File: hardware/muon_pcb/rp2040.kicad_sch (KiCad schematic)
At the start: 38 parts, among them J4 Micro_SD_Card_Det1, J5 Conn_01x02_Pin, SW4 SW_Push_Shielded, SW5 SW_Push_Shielded, U12 RP2040, U3 W25Q128JVS, Y3 ABM8-272-T3

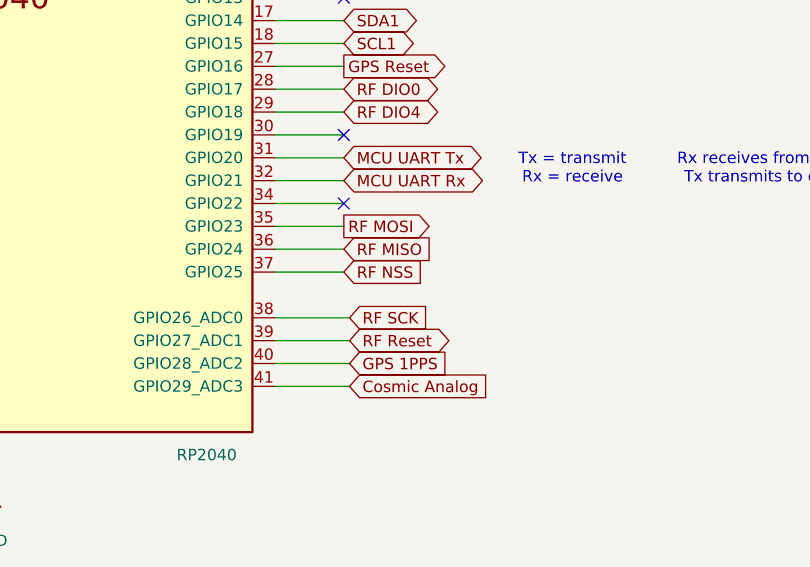
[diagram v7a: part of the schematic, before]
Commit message: cleaned up schematic & implemented changes to layout
to do (off top of my head rn):
-organize project files
-verify design
-maybe check if schematic can be improved again

issues addressed from mikefly's comments:
- ina219 power monitor
- 5v vbus pour near microusb
-gnd pour around crystal oscillator
-removed mounting hole to gnd connection
- corrected microSD orientation and connections
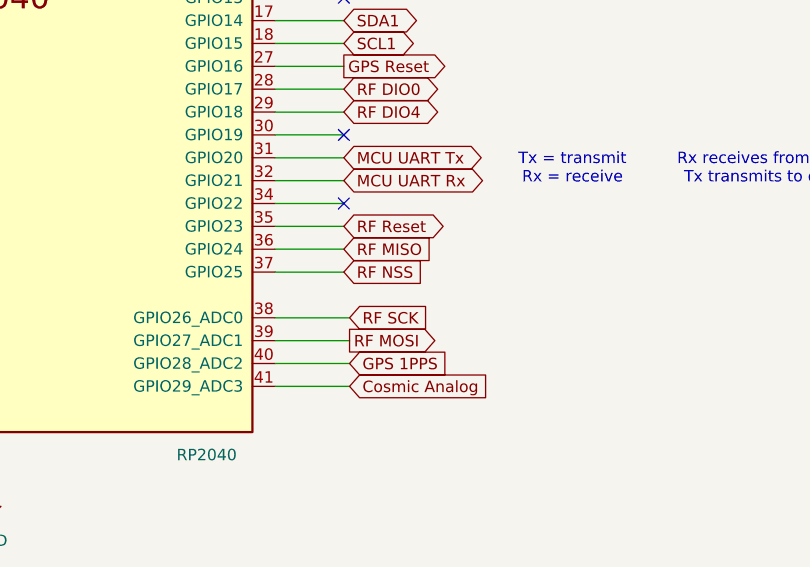
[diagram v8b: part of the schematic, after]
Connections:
- net RF MOSI: now also U12.39 (GPIO27_ADC1); no longer U12.35 (GPIO23)
- net RF Reset: now also U12.35 (GPIO23); no longer U12.39 (GPIO27_ADC1)
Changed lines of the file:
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@@
-		)
-	)
-	(global_label "RF Reset"
-		(shape bidirectional)
-		(at 170.815 198.12 0)
-		(fields_autoplaced yes)
-		(effects
-			(font
-				(size 1.27 1.27)
-			)
-			(justify left)
-		)
-		(property "Intersheetrefs" "${INTERSHEET_REFS}"
-			(at 183.4387 198.12 0)
-			(effects
-				(font
-					(size 1.27 1.27)
-				)
-				(justify left)
-				(hide yes)
-			)
 		)
 	)
@@
 		)
 	)
-	(global_label "RF MOSI"
-		(shape output)
-		(at 170.18 185.42 0)
-		(fields_autoplaced yes)
-		(effects
-			(font
-				(size 1.27 1.27)
-			)
-			(justify left)
-		)
-		(property "Intersheetrefs" "${INTERSHEET_REFS}"
-			(at 181.0876 185.42 0)
-			(effects
-				(font
-					(size 1.27 1.27)
-				)
-				(justify left)
-				(hide yes)
-			)
-		)
-	)
 	(global_label "MicroSD CS"
 		(shape output)
@@
 		)
 	)
+	(global_label "RF MOSI"
+		(shape output)
+		(at 170.815 198.12 0)
+		(fields_autoplaced yes)
+		(effects
+			(font
+				(size 1.27 1.27)
+			)
+			(justify left)
+		)
+		(property "Intersheetrefs" "${INTERSHEET_REFS}"
+			(at 181.7226 198.12 0)
+			(effects
+				(font
+					(size 1.27 1.27)
+				)
+				(justify left)
+				(hide yes)
+			)
+		)
+	)
 	(global_label "GPS 1PPS"
 		(shape input)
@@
 			(effects
 				(font
+					(size 1.27 1.27)
+				)
+				(justify left)
+				(hide yes)
+			)
+		)
+	)
+	(global_label "RF Reset"
+		(shape bidirectional)
+		(at 170.18 185.42 0)
+		(fields_autoplaced yes)
+		(effects
+			(font
+				(size 1.27 1.27)
+			)
+			(justify left)
+		)
+		(property "Intersheetrefs" "${INTERSHEET_REFS}"
+			(at 182.8037 185.42 0)
+			(effects
+				(font
